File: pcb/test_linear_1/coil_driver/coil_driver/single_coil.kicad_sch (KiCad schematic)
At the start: 9 parts, among them Q1 MDD50N03D, U1 VOM617A

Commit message: Before destroying
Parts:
- removed D2: D_Small, symbol Device:D_Small
- removed L1: COIL, symbol Device:L_Small
- added D4: D_Small, symbol Device:D_Small
- D1: MFR (none) -> 599-0210-007F; MOUSER (none) -> 645-599-0210-007F
- D3: MFR (none) -> YQ3LAM10DTR; MOUSER (none) -> 755-YQ3LAM10DTR
- Q1: value MDD50N03D -> BUK6D120; LCSC C5357578 -> (none); MFR MDD50N03D -> BUK6D120-40EX; MOUSER (none) -> 771-BUK6D120-40EX
- U1: MFR VOM617A-6T -> VOM617A-9X001T; MOUSER 78-VOM617A-6T -> 78-VOM617A-9X001T
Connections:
- net IN1: now reaches D3.1 (K)
- net IN1: now also D4.1 (K)
- net IN2: now reaches Q1.1 (D)
- net IN2: now also D4.2 (A)
- net GND1 renamed GND
- net GND2 renamed GNDPWR

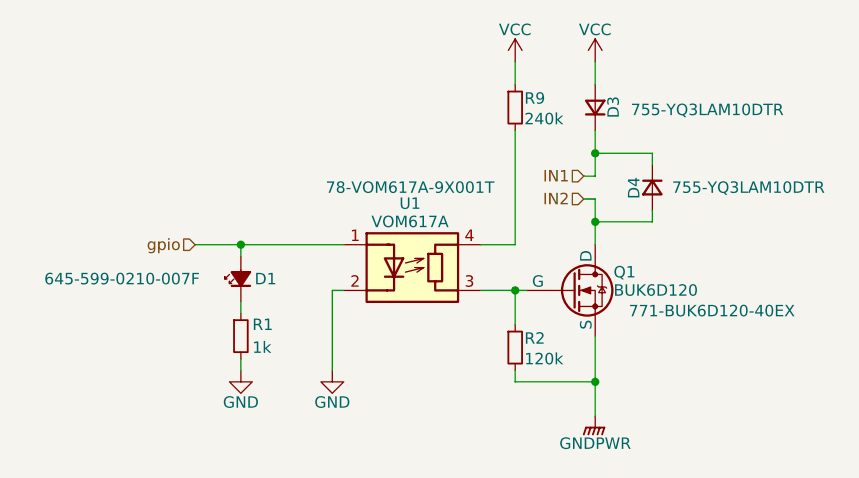
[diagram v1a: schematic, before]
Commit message: Finished schematics and began PCB, only rules for now
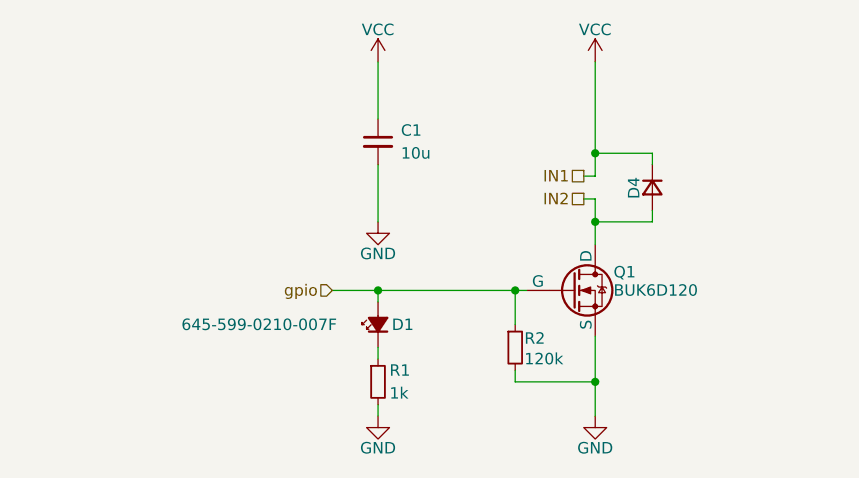
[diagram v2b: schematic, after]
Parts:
- removed D3: D_Small, symbol Device:D_Small
- removed R9: 240k, symbol Device:R_Small
- removed U1: VOM617A, OptoDevice:Luna_NSL-32, symbol Isolator:NSL-32
- added C1: 10u, Capacitor_SMD:C_1206_3216Metric, symbol Device:C_Small
- D1: footprint (none) -> LED_SMD:LED_1206_3216Metric
- D4: footprint (none) -> Diode_SMD:D_SOD-128
- Q1: footprint Package_TO_SOT_SMD:TO-252-2 -> TRANSISTOR:TRANS_BUK9D23-40EX
- R1, R2: footprint (none) -> Resistor_SMD:R_1206_3216Metric
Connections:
- net GNDPWR is gone; now on net GND: Q1.3 (S), R2.2
- net IN1 is gone; now on net VCC: D4.1 (K)
- net GND: now also C1.2
- net VCC: now also C1.1
- net gpio: now also Q1.2 (G), R2.1
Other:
- title: (none) -> Coil driver
- moved on the sheet: D1, R1

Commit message: Began PCB
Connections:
- net GND: now also Q1.4 (S), Q1.8 (S); no longer Q1.3 (S)
- net IN2: now also Q1.2 (D), Q1.5 (D), Q1.6 (D), Q1.7 (D)
- net gpio: now also Q1.3 (G); no longer Q1.2 (G)
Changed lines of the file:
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@@
 		)
 		(property "Footprint" "TRANSISTOR:TRANS_BUK9D23-40EX"
-			(at 110.49 59.69 0)
+			(at 111.252 44.45 0)
 			(effects
 				(font
@@
 		)
 		(property "Datasheet" "https://www.lcsc.com/datasheet/lcsc_datasheet_2305191651_MDD-Microdiode-Electronics-MDD50N03D_C5357578.pdf"
-			(at 105.41 74.93 0)
+			(at 104.902 44.45 0)
 			(effects
 				(font
@@
 		)
 		(property "MOUSER" " 771-BUK6D120-40EX "
-			(at 120.904 64.516 0)
+			(at 118.364 44.958 0)
 			(effects
 				(font
@@
 		)
 		(property "MFR" " BUK6D120-40EX "
-			(at 105.41 62.23 0)
+			(at 106.426 44.45 0)
 			(effects
 				(font
@@
 		(pin "1"
 		)
+		(pin "4"
+		)
+		(pin "8"
+		)
+		(pin "5"
+		)
+		(pin "7"
+		)
+		(pin "6"
+		)
 		(instances
